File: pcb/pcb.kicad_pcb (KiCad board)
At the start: 2 copper layers, 129 parts, among them J1 I2C_Data, J2 SPI_Flash, SW1 Select, SW2 Done, U1 ATmega328P-AU, U2 DessinAfficheur, Y1 16Mhz

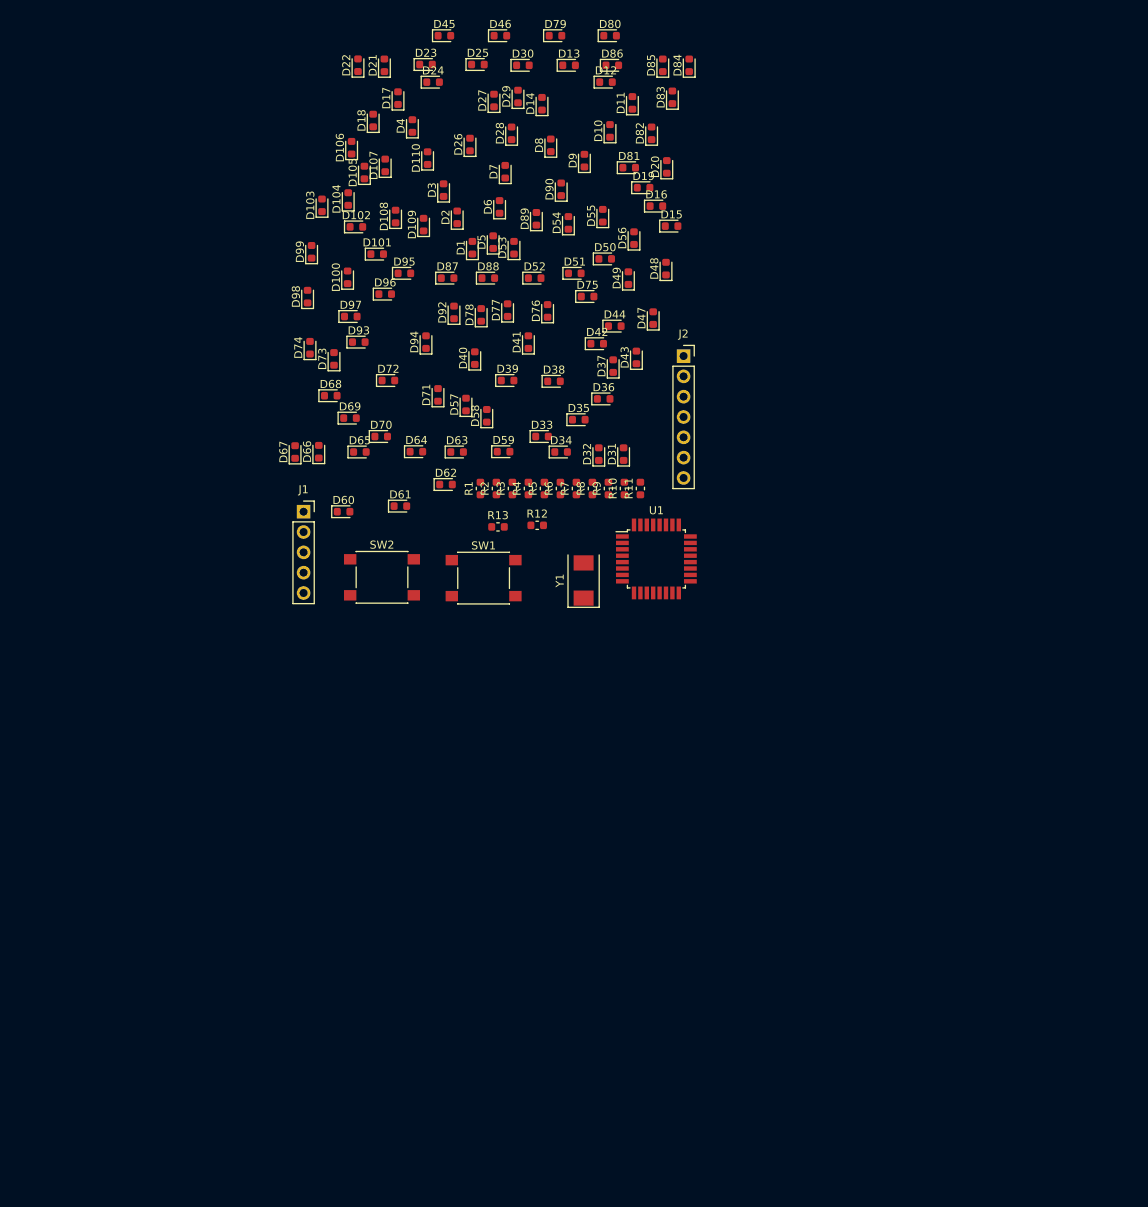
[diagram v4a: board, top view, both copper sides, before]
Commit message: led placement fixed
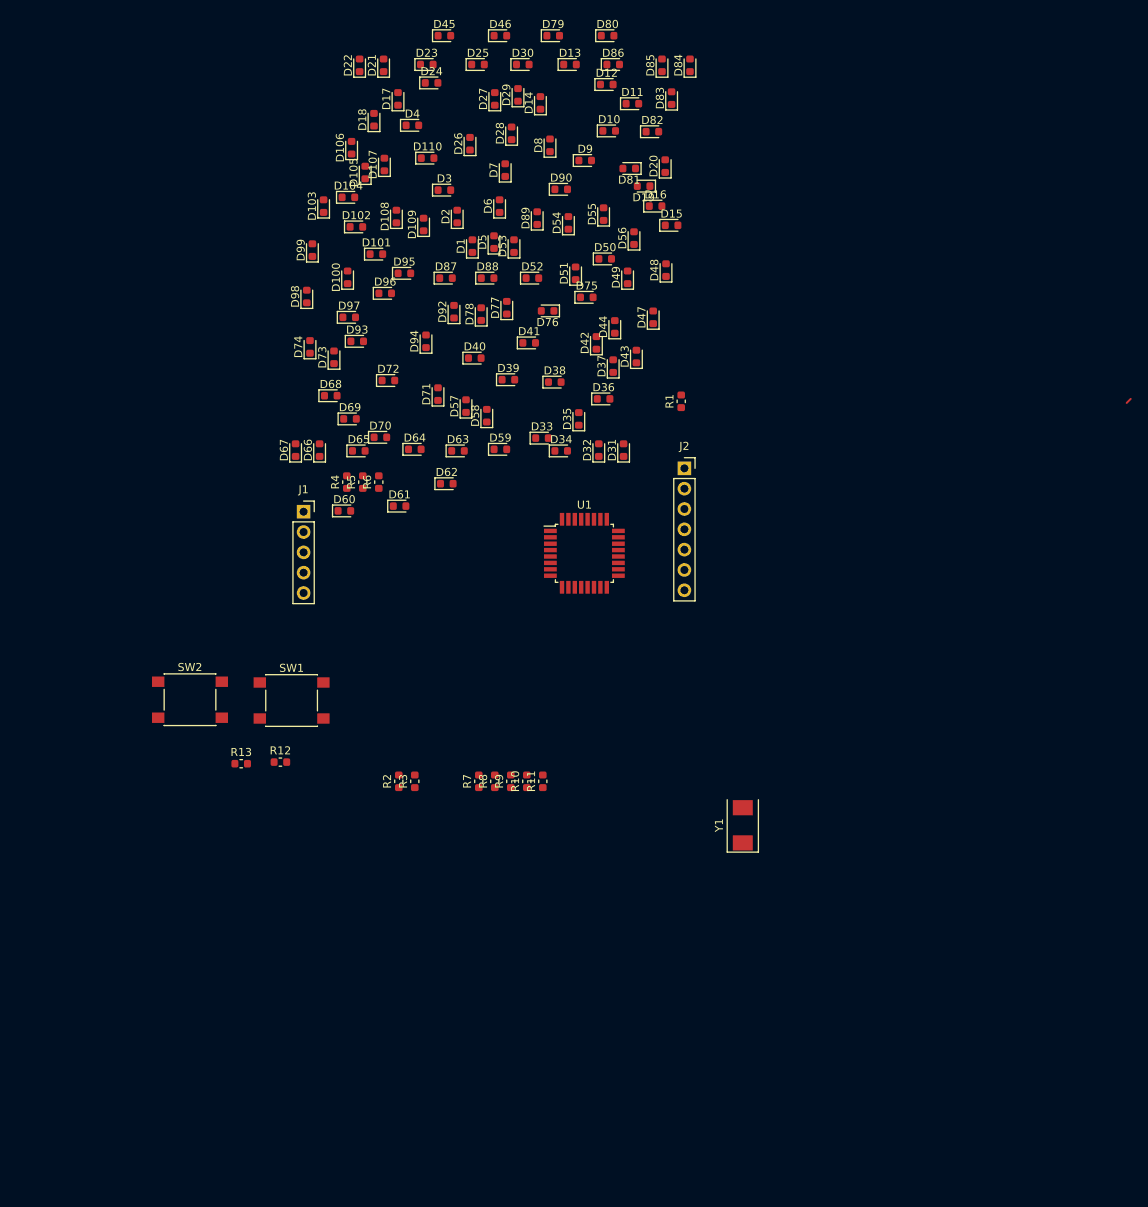
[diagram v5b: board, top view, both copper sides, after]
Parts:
- removed the D31 at (42.7, 53.3)
- removed the D79 at (34.2, 1.00)
- removed the D80 at (41.0, 1.00)
- added D37: L6, LED_SMD:LED_0603_1608Metric, F.Cu at (41.4, 42.3)
- added D38: L2, LED_SMD:LED_0603_1608Metric, F.Cu at (34.1, 44.3)
- added D66: L3, LED_SMD:LED_0603_1608Metric, F.Cu at (4.70, 52.8)
- added U2: DessinAfficheur, pasteur-lib:DessinAfficheurV4.0, F.Cu at (26.4, 30.7)
- moved D11 62.5 mm to (43.8, 9.50)
- moved D80 59.6 mm to (40.7, 1.00)
- moved D13 59.4 mm to (36.0, 4.60), turned to 0 degrees
- moved D12 55.3 mm to (40.6, 7.10)
- moved D24 53.0 mm to (18.7, 6.90)
- moved D79 52.6 mm to (33.9, 1.00), turned to 0 degrees
- moved D15 52.4 mm to (48.7, 24.7), turned to 0 degrees
- moved D67 50.2 mm to (1.70, 52.8)
- moved D85 49.0 mm to (47.5, 4.70)
- moved D57 44.7 mm to (23.0, 47.3)
- moved D63 44.7 mm to (22.0, 52.9), turned to 0 degrees
- moved D36 44.5 mm to (40.2, 46.4), turned to 0 degrees
- moved R12 43.7 mm to (-0.20, 91.8)
- moved R13 43.7 mm to (-5.10, 92.0)
- moved D84 43.0 mm to (51.0, 4.70), turned to 90 degrees
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- renumbered D4 to D1, D18 to D10, D5 to D100, D33 to D101, D29 to D102, D41 to D103, D35 to D104, D97 to D105, D53 to D106, D95 to D107, D20 to D108, D54 to D109, D60 to D11, D81 to D110, D65 to D12, D67 to D13, D30 to D14, D66 to D15, D17 to D16, D37 to D17, D85 to D18, D48 to D19, D6 to D2, D11 to D20, D104 to D21, D74 to D22, D12 to D23, D61 to D24, D98 to D25, D99 to D26, D15 to D27, D83 to D28, D25 to D29, D13 to D3, D72 to D30, D76 to D31, D77 to D32, D16 to D33, D47 to D34, D90 to D35, D106 to D36, D78 to D39, D24 to D4, D59 to D40, D52 to D41, D108 to D42, D26 to D43, D55 to D44, D3 to D47, D105 to D48, D8 to D49, D63 to D5, D21 to D50, D88 to D51, D28 to D52, D19 to D53, D56 to D54, D109 to D55, D43 to D56, D22 to D57, D103 to D58, D34 to D59, D86 to D6, D69 to D60, D58 to D61, D51 to D62, D14 to D63, D73 to D64, D44 to D65, D27 to D67, D94 to D68, D100 to D69, D84 to D7, D7 to D70, D107 to D71, D89 to D72, D68 to D73, D71 to D74, D39 to D75, D49 to D76, D50 to D77, D10 to D78, D32 to D79, D23 to D8, D62 to D80, D82 to D81, D102 to D82, D9 to D83, D38 to D84, D57 to D85, D75 to D86, D92 to D87, D1 to D88, D101 to D89, D64 to D9, D42 to D90, D96 to D92, D110 to D93, D2 to D94, D36 to D95, D40 to D96, D87 to D97, D70 to D98, D93 to D99
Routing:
- net Net-(D1-Pad1): track 0.00 -> 0.71 mm

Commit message: routing v1
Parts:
- J2: moved to B.Cu
- moved R10 67.5 mm to (51.6, 30.1)
- moved R3 51.6 mm to (45.2, 51.2)
- moved R2 45.7 mm to (13.9, 48.5), turned to 180 degrees
- moved R11 42.2 mm to (10.9, 58.0), turned to 180 degrees
- moved R4 41.1 mm to (47.1, 43.8), turned to 180 degrees
- moved R13 40.2 mm to (24.1, 64.3), turned to 180 degrees
- moved R12 40.0 mm to (28.9, 64.3), turned to 180 degrees
- moved R8 39.8 mm to (14.8, 56.2), turned to 180 degrees
- moved R5 39.7 mm to (46.4, 40.8)
- moved SW2 38.4 mm to (23.8, 68.8)
- moved R6 36.5 mm to (47.0, 46.1), turned to 180 degrees
- moved R7 34.1 mm to (20.6, 60.3), turned to 180 degrees
- moved R9 32.1 mm to (20.6, 63.1), turned to 180 degrees
- moved Y1 22.3 mm to (46.2, 80.5), turned to 0 degrees
- moved SW1 18.6 mm to (11.8, 68.8)
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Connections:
- net Net-(D1-Pad1) renamed /NL01
- net Net-(D1-Pad2) renamed /NL02
- net Net-(D10-Pad1) renamed /NL04
- net Net-(D100-Pad1) renamed /NL11
- net Net-(D100-Pad2) renamed /NL06
- net Net-(D101-Pad1) renamed /NL05
- net Net-(D105-Pad1) renamed /NL03
- net Net-(D31-Pad2) renamed /NL07
- net Net-(D43-Pad2) renamed /NL08
- net Net-(D57-Pad2) renamed /NL09
- net Net-(D73-Pad2) renamed /NL10
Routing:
- net /NL04: track 0.00 -> 240.4 mm, vias 0 -> 8
- net /NL03: track 0.00 -> 220.4 mm, vias 0 -> 11
- net /NL08: track 0.00 -> 196.0 mm, vias 0 -> 7
- net /NL06: track 0.00 -> 187.1 mm, vias 0 -> 5
- net /NL05: track 0.00 -> 180.7 mm, vias 0 -> 6
- net /NL01: track 0.71 -> 172.5 mm, vias 0 -> 7
- net /NL10: track 0.00 -> 165.0 mm, vias 0 -> 5
- net /NL07: track 0.00 -> 155.6 mm, vias 0 -> 4
- net /NL02: track 0.00 -> 152.3 mm, vias 0 -> 7
- net /NL11: track 0.00 -> 124.7 mm, vias 0 -> 4
- net /NL09: track 0.00 -> 120.9 mm
- net Net-(J1-Pad1): track 0.00 -> 118.1 mm, vias 0 -> 2
- net GND: track 0.00 -> 76.0 mm, vias 0 -> 2
- net Net-(J1-Pad2): track 0.00 -> 63.7 mm, vias 0 -> 2
- net Net-(J1-Pad4): track 0.00 -> 50.7 mm, vias 0 -> 2
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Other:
- board text added: "Ceci n'est pas un quartz"

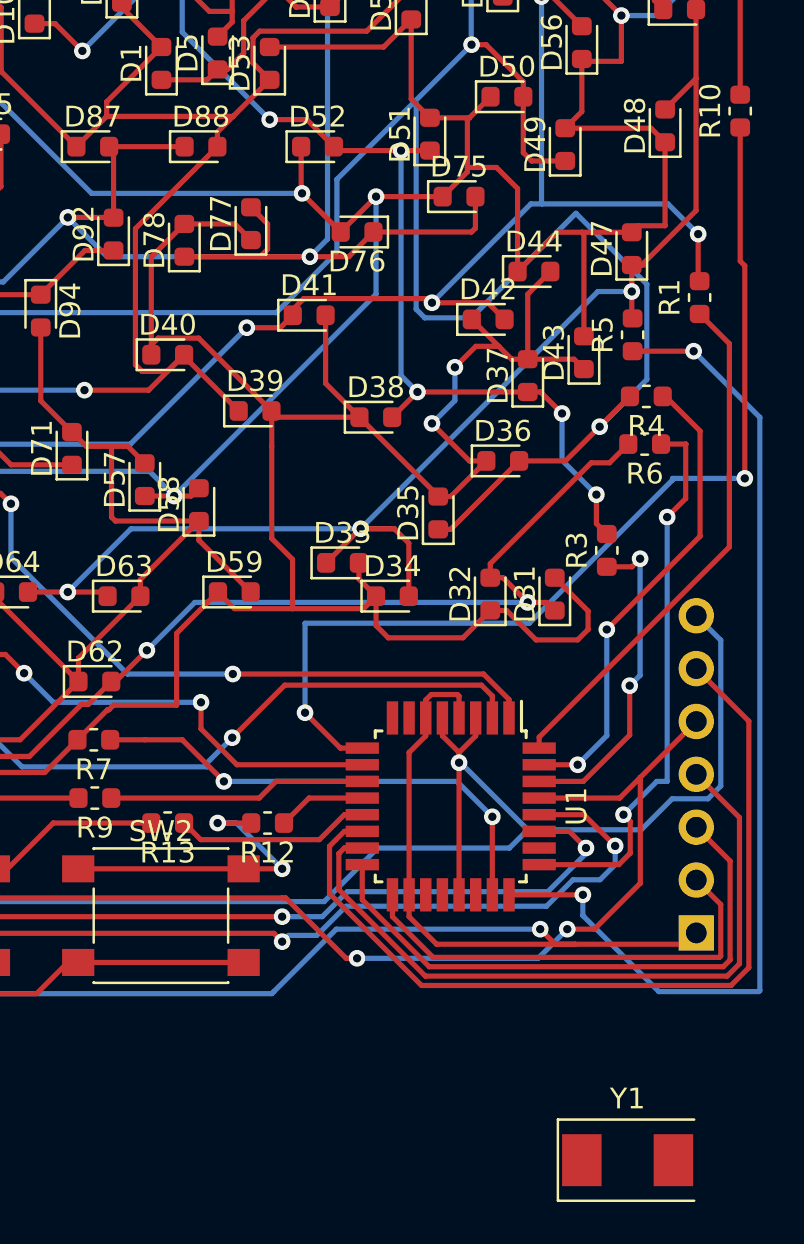
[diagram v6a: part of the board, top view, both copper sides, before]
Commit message: add crystal to the pcb
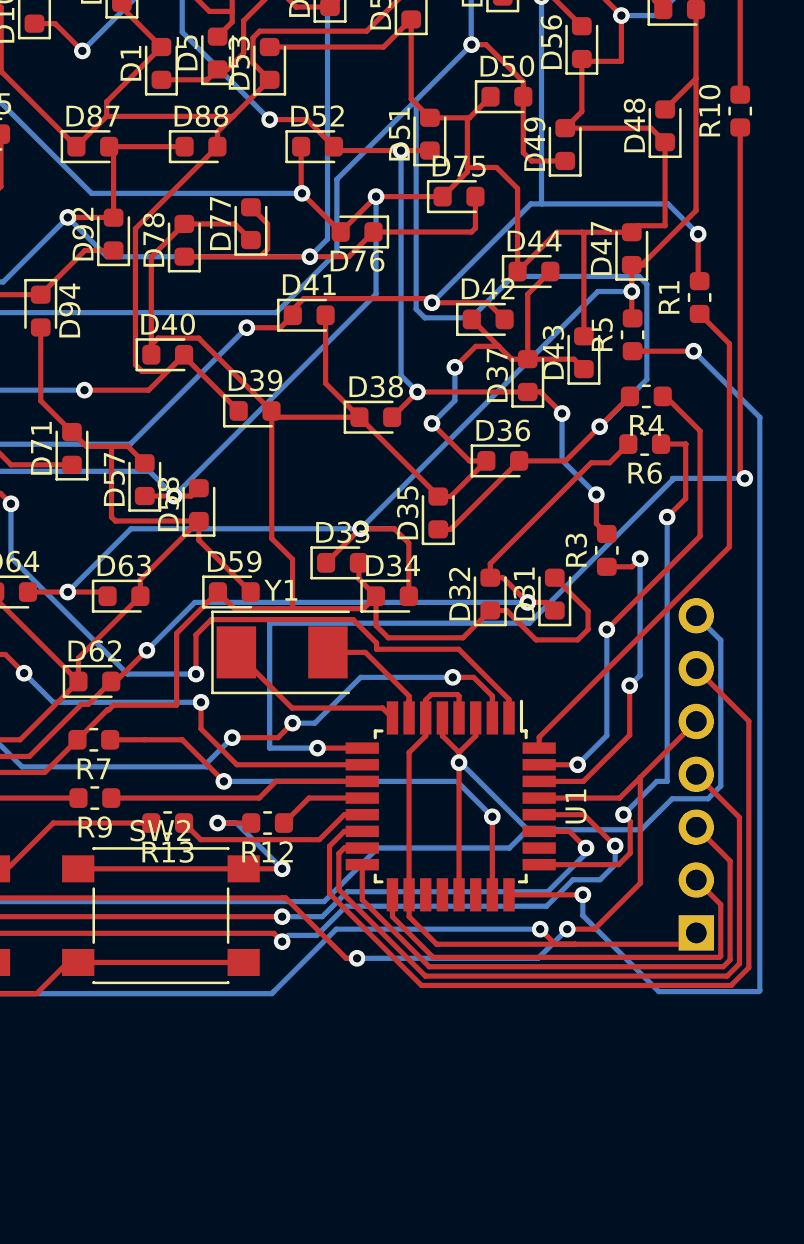
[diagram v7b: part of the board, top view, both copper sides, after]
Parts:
- moved Y1 29.5 mm to (29.6, 56.1)
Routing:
- net Net-(U1-Pad8): track 0.00 -> 8.80 mm
- net Net-(U1-Pad7): track 0.00 -> 6.68 mm
- net Net-(R10-Pad1): track 48.8 -> 53.2 mm
- net Net-(R2-Pad1): track 32.3 -> 35.7 mm
- net /NL04: track 240.4 -> 237.9 mm
- net Net-(R11-Pad1): track 32.5 -> 32.8 mm, vias 2 -> 4
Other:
- board text removed: "Ceci n'est pas un quartz"

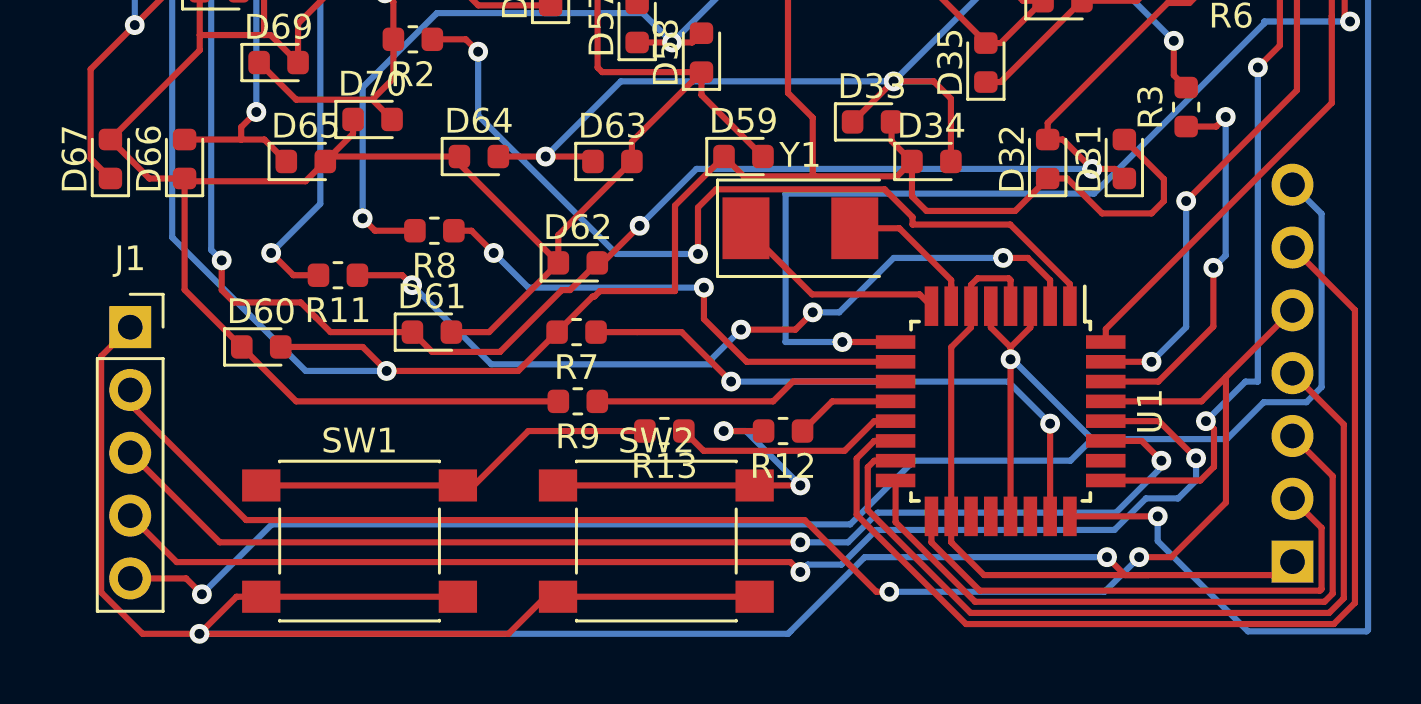
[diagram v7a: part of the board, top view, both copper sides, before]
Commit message: reverse orientation spi / i2c
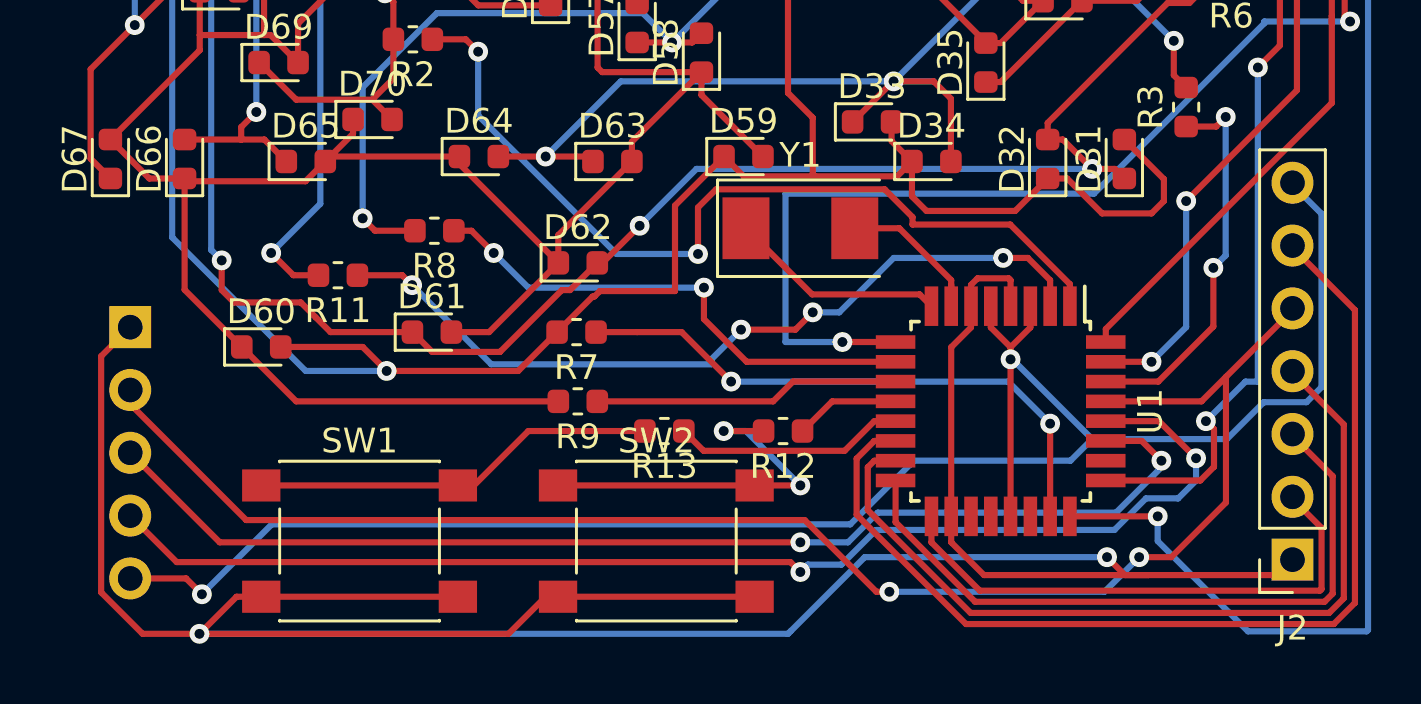
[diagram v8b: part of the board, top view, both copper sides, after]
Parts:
- J1: moved to B.Cu
- J2: moved to F.Cu
- moved J2 0.08 mm to (49.5, 69.5), turned to 180 degrees
- turned J1 to 180 degrees
